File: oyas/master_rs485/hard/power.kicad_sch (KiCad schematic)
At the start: 25 parts, among them J1 POWER_12V, J5 Leds RGB, Q1 BPC_2N2222A, Q3 BC327, U2 BPC_Alim5V, U5 LM1117DT-3.3

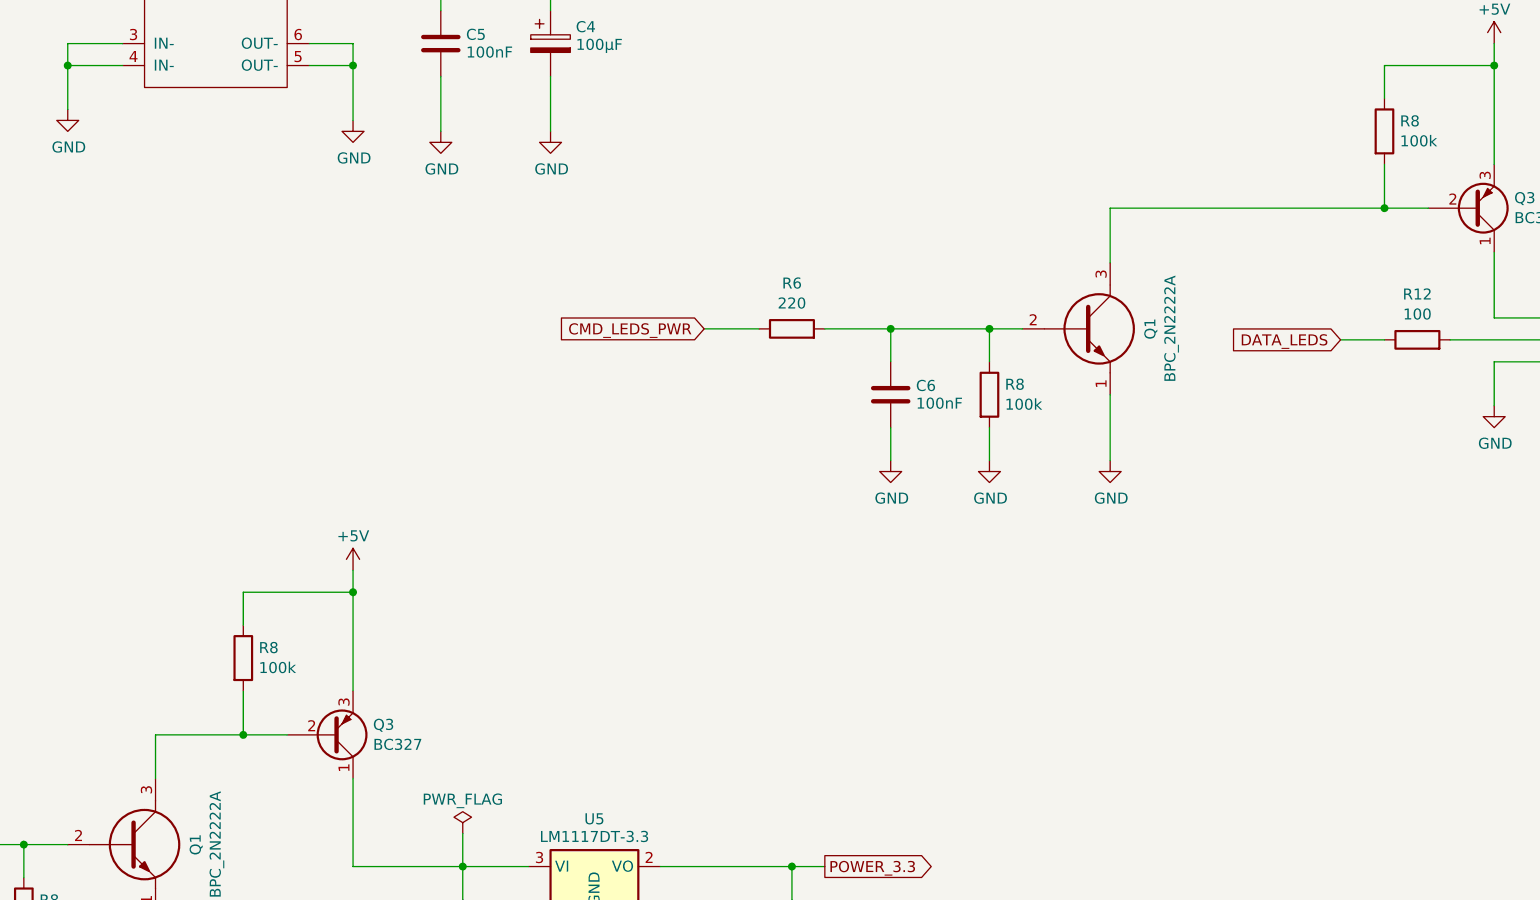
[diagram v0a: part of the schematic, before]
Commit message: MAJ correction limitation du courant de base des pnp (Pwr Wifi et LEDs)
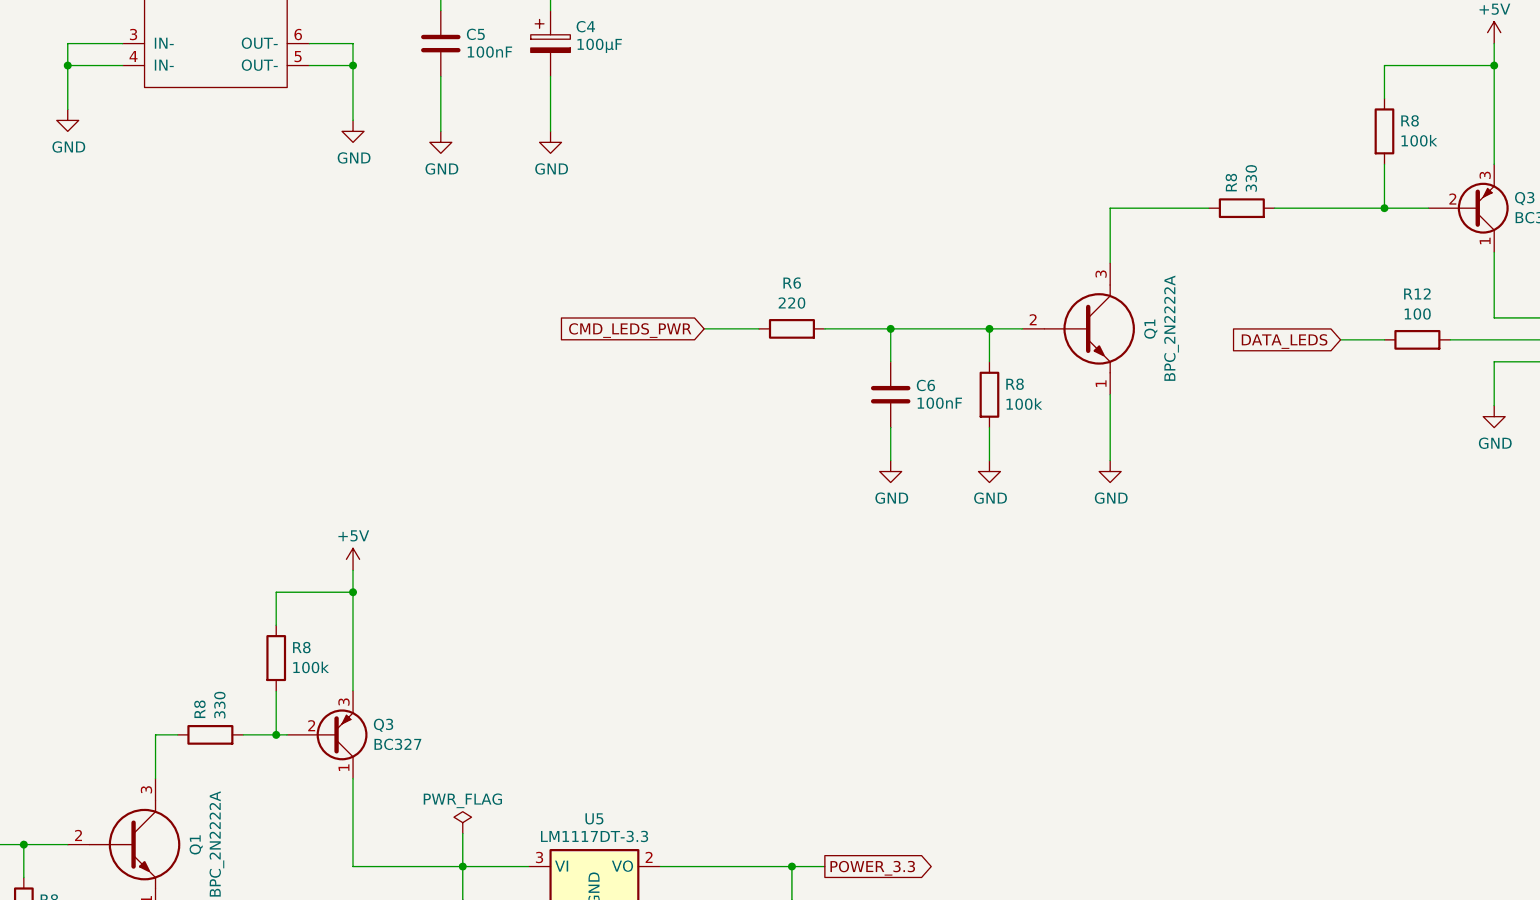
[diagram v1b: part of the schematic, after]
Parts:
- added R8 (x2): 330, Resistor_THT:R_Axial_DIN0204_L3.6mm_D1.6mm_P7.62mm_Horizontal, symbol Device:R
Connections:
- net at Q3.2 (B), R8.2: now also R8.2; no longer Q1.3 (x2)
- new net: Q1.3, R8.1 (x2)
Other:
- moved on the sheet: R8
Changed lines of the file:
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@@
     (comment 2 "Inteface LEDs RGB - Bouton - RTC")
     (comment 3 "Alim 12V - Sortie 12V pilotable - Bus RS485")
+    (comment 4 "Maître RS485 avec alim 12 V commutée")
+  )
+  (junction (at 92.71 143.51) (diameter 0) (color 0 0 0 0)
   )
   (junction (at 175.26 96.52) (diameter 0) (color 0 0 0 0)
   )
+  (junction (at 250.19 95.25) (diameter 0) (color 0 0 0 0)
+  )
+  (junction (at 152.4 158.75) (diameter 0) (color 0 0 0 0)
+  )
+  (junction (at 101.6 127) (diameter 0) (color 0 0 0 0)
+  )
+  (junction (at 101.6 66.04) (diameter 0) (color 0 0 0 0)
+  )
+  (junction (at 68.58 66.04) (diameter 0) (color 0 0 0 0)
+  )
+  (junction (at 233.68 66.04) (diameter 0) (color 0 0 0 0)
+  )
   (junction (at 220.98 82.55) (diameter 0) (color 0 0 0 0)
   )
-  (junction (at 250.19 95.25) (diameter 0) (color 0 0 0 0)
-  )
-  (junction (at 152.4 158.75) (diameter 0) (color 0 0 0 0)
-  )
-  (junction (at 101.6 127) (diameter 0) (color 0 0 0 0)
-  )
-  (junction (at 101.6 66.04) (diameter 0) (color 0 0 0 0)
-  )
-  (junction (at 68.58 66.04) (diameter 0) (color 0 0 0 0)
-  )
-  (junction (at 233.68 66.04) (diameter 0) (color 0 0 0 0)
-  )
   (junction (at 68.58 54.61) (diameter 0) (color 0 0 0 0)
   )
@@
   (junction (at 63.5 156.21) (diameter 0) (color 0 0 0 0)
   )
-  (junction (at 88.9 143.51) (diameter 0) (color 0 0 0 0)
-  )
   (junction (at 111.76 54.61) (diameter 0) (color 0 0 0 0)
   )
@@
     (stroke (width 0) (type default))
   )
-  (wire (pts (xy 88.9 138.43) (xy 88.9 143.51))
+  (wire (pts (xy 92.71 138.43) (xy 92.71 143.51))
     (stroke (width 0) (type default))
   )
@@
     (stroke (width 0) (type default))
   )
+  (wire (pts (xy 189.23 82.55) (xy 200.66 82.55))
+    (stroke (width 0) (type default))
+  )
   (wire (pts (xy 68.58 63.5) (xy 68.58 66.04))
     (stroke (width 0) (type default))
@@
     (stroke (width 0) (type default))
   )
-  (wire (pts (xy 101.6 127) (xy 88.9 127))
+  (wire (pts (xy 101.6 127) (xy 92.71 127))
     (stroke (width 0) (type default))
   )
@@
     (stroke (width 0) (type default))
   )
+  (wire (pts (xy 88.9 143.51) (xy 92.71 143.51))
+    (stroke (width 0) (type default))
+  )
   (wire (pts (xy 96.52 55.88) (xy 101.6 55.88))
     (stroke (width 0) (type default))
@@
     (stroke (width 0) (type default))
   )
+  (wire (pts (xy 78.74 143.51) (xy 81.28 143.51))
+    (stroke (width 0) (type default))
+  )
   (wire (pts (xy 101.6 53.34) (xy 101.6 54.61))
     (stroke (width 0) (type default))
@@
     (stroke (width 0) (type default))
   )
-  (wire (pts (xy 88.9 143.51) (xy 78.74 143.51))
-    (stroke (width 0) (type default))
-  )
   (wire (pts (xy 68.58 54.61) (xy 68.58 55.88))
     (stroke (width 0) (type default))
@@
     (stroke (width 0) (type default))
   )
+  (wire (pts (xy 208.28 82.55) (xy 220.98 82.55))
+    (stroke (width 0) (type default))
+  )
   (wire (pts (xy 250.19 90.17) (xy 250.19 95.25))
     (stroke (width 0) (type default))
@@
     (stroke (width 0) (type default))
   )
-  (wire (pts (xy 88.9 127) (xy 88.9 130.81))
+  (wire (pts (xy 92.71 127) (xy 92.71 130.81))
     (stroke (width 0) (type default))
   )
@@
     (stroke (width 0) (type default))
   )
-  (wire (pts (xy 88.9 143.51) (xy 93.98 143.51))
+  (wire (pts (xy 92.71 143.51) (xy 93.98 143.51))
     (stroke (width 0) (type default))
   )
@@
   )
   (wire (pts (xy 63.5 156.21) (xy 63.5 160.02))
-    (stroke (width 0) (type default))
-  )
-  (wire (pts (xy 220.98 82.55) (xy 189.23 82.55))
     (stroke (width 0) (type default))
   )
@@
     )
   )
+  (symbol (lib_id "Device:R") (at 85.09 143.51 90) (unit 1)
+    (in_bom yes) (on_board yes) (dnp no)
+    (property "Reference" "R8" (at 83.9216 141.732 0)
+      (effects (font (size 1.27 1.27)) (justify left))
+    )
+    (property "Value" "330" (at 86.233 141.732 0)
+      (effects (font (size 1.27 1.27)) (justify left))
+    )
+    (property "Footprint" "Resistor_THT:R_Axial_DIN0204_L3.6mm_D1.6mm_P7.62mm_Horizontal" (at 85.09 145.288 90)
+      (effects (font (size 1.27 1.27)) hide)
+    )
+    (property "Datasheet" "~" (at 85.09 143.51 0)
+      (effects (font (size 1.27 1.27)) hide)
+    )
+    (pin "1")
+    (pin "2")
+    (instances
+      (project "board_rs485_master"
+        (path "/27904310-f1aa-47e2-a2a6-8db936442bd1"
+          (reference "R8") (unit 1)
+        )
+        (path "/27904310-f1aa-47e2-a2a6-8db936442bd1/2eaa2441-998c-4f1a-b526-09e479f565d5"
+          (reference "R20") (unit 1)
+        )
+      )
+    )
+  )
   (symbol (lib_id "power:GND") (at 163.83 111.76 0) (unit 1)
     (in_bom yes) (on_board yes) (dnp no)
@@
     )
   )
+  (symbol (lib_id "Device:R") (at 204.47 82.55 90) (unit 1)
+    (in_bom yes) (on_board yes) (dnp no)
+    (property "Reference" "R8" (at 203.3016 80.772 0)
+      (effects (font (size 1.27 1.27)) (justify left))
+    )
+    (property "Value" "330" (at 205.613 80.772 0)
+      (effects (font (size 1.27 1.27)) (justify left))
+    )
+    (property "Footprint" "Resistor_THT:R_Axial_DIN0204_L3.6mm_D1.6mm_P7.62mm_Horizontal" (at 204.47 84.328 90)
+      (effects (font (size 1.27 1.27)) hide)
+    )
+    (property "Datasheet" "~" (at 204.47 82.55 0)
+      (effects (font (size 1.27 1.27)) hide)
+    )
+    (pin "1")
+    (pin "2")
+    (instances
+      (project "board_rs485_master"
+        (path "/27904310-f1aa-47e2-a2a6-8db936442bd1"
+          (reference "R8") (unit 1)
+        )
+        (path "/27904310-f1aa-47e2-a2a6-8db936442bd1/2eaa2441-998c-4f1a-b526-09e479f565d5"
+          (reference "R21") (unit 1)
+        )
+      )
+    )
+  )
   (symbol (lib_id "power:+5V") (at 233.68 63.5 0) (unit 1)
     (in_bom yes) (on_board yes) (dnp no) (fields_autoplaced)
@@
     )
   )
-  (symbol (lib_id "Device:R") (at 88.9 134.62 0) (unit 1)
-    (in_bom yes) (on_board yes) (dnp no)
-    (property "Reference" "R8" (at 90.678 133.4516 0)
-      (effects (font (size 1.27 1.27)) (justify left))
-    )
-    (property "Value" "100k" (at 90.678 135.763 0)
-      (effects (font (size 1.27 1.27)) (justify left))
-    )
-    (property "Footprint" "Resistor_THT:R_Axial_DIN0204_L3.6mm_D1.6mm_P7.62mm_Horizontal" (at 87.122 134.62 90)
-      (effects (font (size 1.27 1.27)) hide)
-    )
-    (property "Datasheet" "~" (at 88.9 134.62 0)
-      (effects (font (size 1.27 1.27)) hide)
-    )
+  (symbol (lib_id "Device:R") (at 92.71 134.62 0) (unit 1)
+    (in_bom yes) (on_board yes) (dnp no)
+    (property "Reference" "R8" (at 94.488 133.4516 0)
+      (effects (font (size 1.27 1.27)) (justify left))
+    )
+    (property "Value" "100k" (at 94.488 135.763 0)
+      (effects (font (size 1.27 1.27)) (justify left))
+    )
+    (property "Footprint" "Resistor_THT:R_Axial_DIN0204_L3.6mm_D1.6mm_P7.62mm_Horizontal" (at 90.932 134.62 90)
+      (effects (font (size 1.27 1.27)) hide)
+    )
+    (property "Datasheet" "~" (at 92.71 134.62 0)
+      (effects (font (size 1.27 1.27)) hide)
+    )

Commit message: Quelques commentaires sur le schéma pour préparer la version 2027...
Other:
- note added: "Ajouter une TVS 18V 600W sur le 12V à l'entrée (cf carte Oya M0)"
- note added: "Mettre des capas en entrée. C'est pourquoi Ca marchait pas !!!"
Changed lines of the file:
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@@
     (effects (font (size 5.08 5.08) (thickness 2.54) bold) (justify left bottom))
+  )
+  (text "Ajouter une TVS 18V 600W sur le 12V à l'entrée (cf carte Oya M0)"
+    (at 29.21 86.995 0)
+    (effects (font (size 1.27 1.27)) (justify left bottom))
+  )
+  (text "Mettre des capas en entrée.\nC'est pourquoi Ca marchait pas !!!"
+    (at 27.94 69.215 0)
+    (effects (font (size 1.27 1.27)) (justify left bottom))
   )
   (global_label "DATA_LEDS" (shape input) (at 215.9 97.79 180)
